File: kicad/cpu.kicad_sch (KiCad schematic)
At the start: 11 parts, among them IC1 Z180, U31 GAL16V8, U8 74HC138, Y2 12.288 MHz

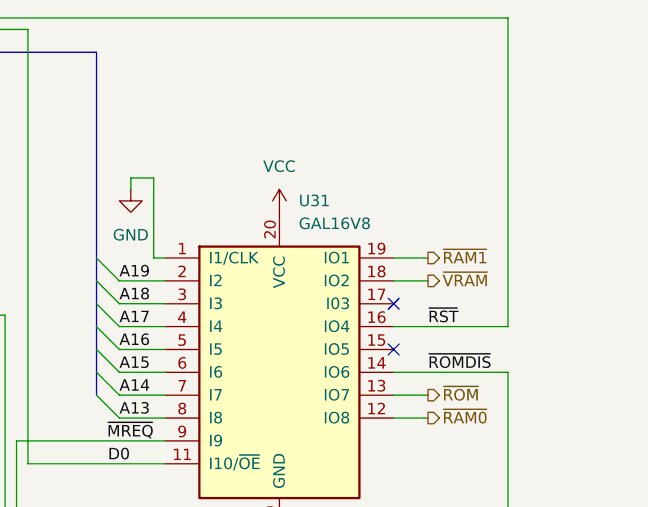
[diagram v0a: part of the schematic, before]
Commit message: hw: add RC to /RD for CF for increased compatibility
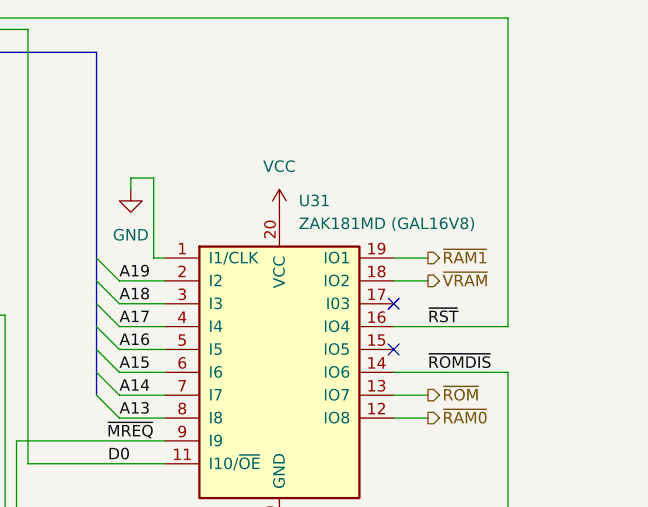
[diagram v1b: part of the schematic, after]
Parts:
- U31: value GAL16V8 -> ZAK181MD (GAL16V8)
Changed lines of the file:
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@@
 			)
 		)
-		(property "Value" "GAL16V8"
+		(property "Value" "ZAK181MD (GAL16V8)"
 			(at 243.4433 59.69 0)
 			(effects
